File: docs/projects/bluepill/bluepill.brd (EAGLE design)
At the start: 89.8 x 49.5 mm, 10 parts

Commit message: bluepill
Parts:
- moved SV2 5.08 mm to (41.9, 35.6)
- moved S1 1.27 mm to (7.62, 47.0)
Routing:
- net GND: track 156.3 -> 167.6 mm
- net D12: track 81.3 -> 91.4 mm
- net RESET: track 107.6 -> 113.9 mm
- net D11: track 86.4 -> 91.4 mm
- net N$8: track 7.62 -> 12.7 mm
- net N$7: track 7.62 -> 12.7 mm
- net N$6: track 7.62 -> 12.7 mm
- net N$5: track 7.62 -> 12.7 mm
- net N$4: track 7.62 -> 12.7 mm
- net N$3: track 7.62 -> 12.7 mm
- net N$1: track 7.62 -> 12.7 mm
- net D6: track 63.7 -> 66.0 mm
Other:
- board size 89.8 x 49.5 mm -> 88.6 x 48.2 mm

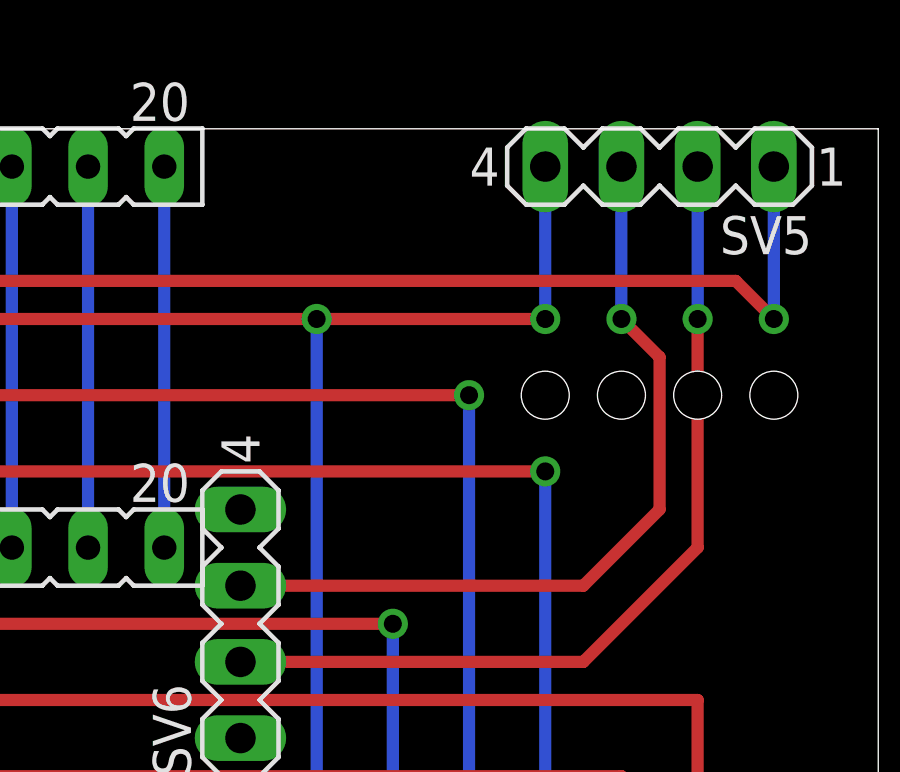
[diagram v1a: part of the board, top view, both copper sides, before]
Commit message: bluepill: fix order
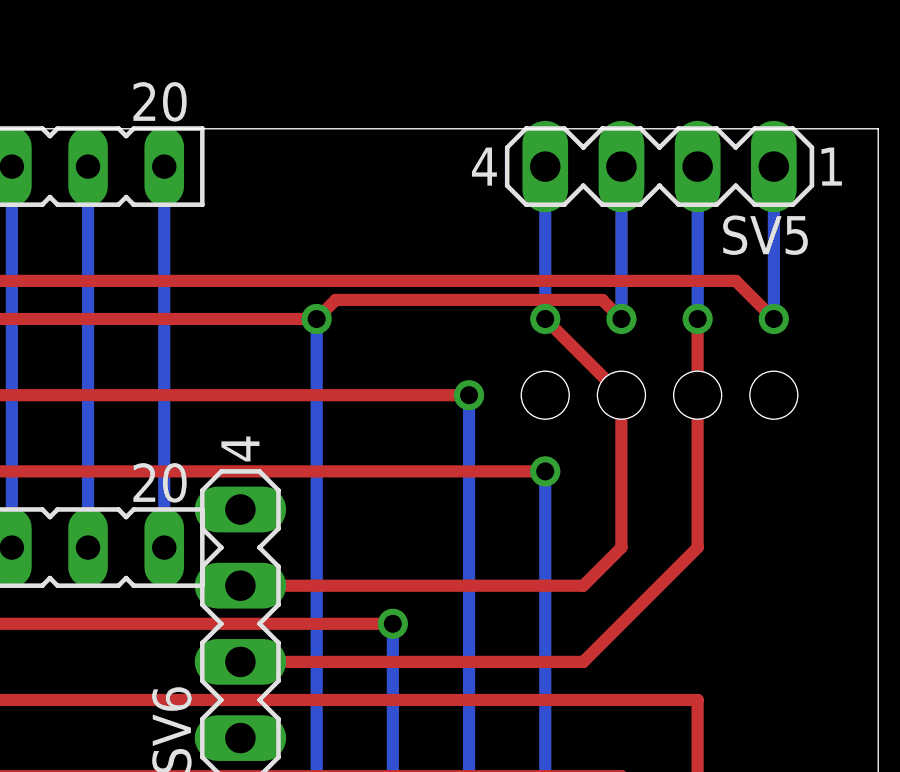
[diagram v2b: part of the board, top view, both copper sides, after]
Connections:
- net DCLK: now also SV5.4; no longer SV5.3
- net GND: now also SV5.3; no longer SV5.4
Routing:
- net GND: track 167.6 -> 170.7 mm
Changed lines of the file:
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@@
 <wire x1="10.16" y1="38.1" x2="10.16" y2="46.6852" width="0.4064" layer="16"/>
 <wire x1="10.16" y1="46.6852" x2="9.8806" y2="48.2346" width="0.4064" layer="16"/>
-<contactref element="SV5" pad="4"/>
-<wire x1="78.74" y1="48.26" x2="78.74" y2="43.18" width="0.4064" layer="16"/>
-<via x="78.74" y="43.18" extent="1-16" drill="0.6" shape="square"/>
+<via x="81.28" y="43.18" extent="1-16" drill="0.6" shape="square"/>
 <via x="20.32" y="43.18" extent="1-16" drill="0.6" shape="square"/>
 <wire x1="71.12" y1="43.18" x2="20.32" y2="43.18" width="0.4064" layer="1"/>
@@
 <wire x1="71.12" y1="22.86" x2="71.12" y2="43.18" width="0.4064" layer="16"/>
 <via x="71.12" y="43.18" extent="1-16" drill="0.6" shape="square"/>
-<wire x1="71.12" y1="43.18" x2="78.74" y2="43.18" width="0.4064" layer="1"/>
+<contactref element="SV5" pad="3"/>
+<wire x1="81.28" y1="48.26" x2="81.28" y2="43.18" width="0.4064" layer="16"/>
+<wire x1="71.12" y1="43.18" x2="71.755" y2="43.815" width="0.4064" layer="1"/>
+<wire x1="71.755" y1="43.815" x2="80.645" y2="43.815" width="0.4064" layer="1"/>
+<wire x1="80.645" y1="43.815" x2="81.28" y2="43.18" width="0.4064" layer="1"/>
 </signal>
 <signal name="VCC">
@@
 </signal>
 <signal name="DCLK">
-<contactref element="SV5" pad="3"/>
 <contactref element="SV6" pad="3"/>
-<wire x1="68.58" y1="34.29" x2="80.01" y2="34.29" width="0.4064" layer="1"/>
-<wire x1="80.01" y1="34.29" x2="82.55" y2="36.83" width="0.4064" layer="1"/>
-<wire x1="82.55" y1="36.83" x2="82.55" y2="41.91" width="0.4064" layer="1"/>
-<wire x1="82.55" y1="41.91" x2="81.28" y2="43.18" width="0.4064" layer="1"/>
-<via x="81.28" y="43.18" extent="1-16" drill="0.6" shape="square"/>
-<wire x1="81.28" y1="43.18" x2="81.28" y2="48.26" width="0.4064" layer="16"/>
+<contactref element="SV5" pad="4"/>
+<wire x1="78.74" y1="48.26" x2="78.74" y2="43.18" width="0.4064" layer="16"/>
+<via x="78.74" y="43.18" extent="1-16" drill="0.6" shape="square"/>
+<wire x1="78.74" y1="43.18" x2="81.28" y2="40.64" width="0.4064" layer="1"/>
+<wire x1="81.28" y1="40.64" x2="81.28" y2="35.56" width="0.4064" layer="1"/>
+<wire x1="81.28" y1="35.56" x2="80.01" y2="34.29" width="0.4064" layer="1"/>
+<wire x1="80.01" y1="34.29" x2="68.58" y2="34.29" width="0.4064" layer="1"/>
 </signal>
 </signals>
